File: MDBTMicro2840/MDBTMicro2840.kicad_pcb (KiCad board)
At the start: 2 copper layers, 33 x 18 mm, 25 parts, among them J1 USB_C_Receptacle_USB2.0, J2 SWD, U1 XC6220B331MR-G, U2 MDBT50Q-x1MV2, U3 TP4057, U4 ProMicro, X1 32.768kHz

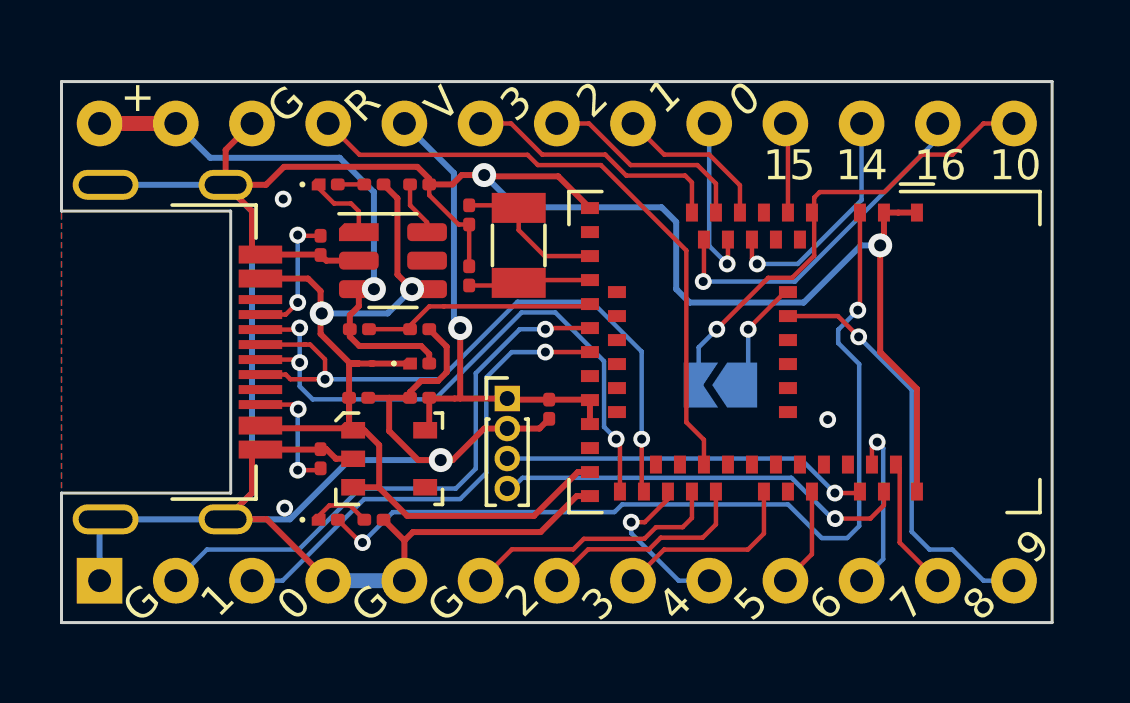
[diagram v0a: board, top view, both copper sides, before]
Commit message: Update 1N5819 footprint to SOD123
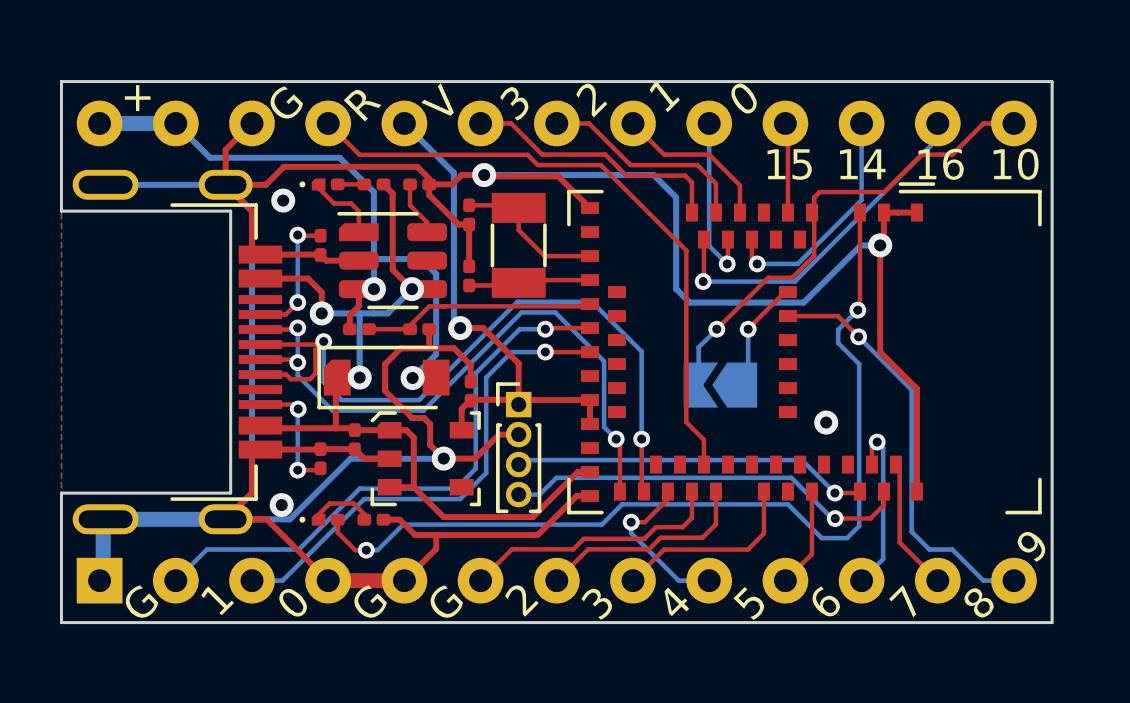
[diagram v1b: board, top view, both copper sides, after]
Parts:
- removed the C3 at (147.1, 103.5)
- D1: footprint Diode_SMD:D_0201_0603Metric -> Diode_SMD:D_SOD-123
- moved C4 1.72 mm to (144.4, 102.9), turned to -90 degrees
- moved C3 1.40 mm to (140.6, 104.5), turned to 90 degrees
- moved U1 1.22 mm to (142.9, 105.2)
- moved D1 1.19 mm to (141.7, 102.5)
- moved J2 0.43 mm to (146.1, 103.3)
- renumbered C4 to C3, C5 to C4, U3 to U2, U2 to U3
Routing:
- net VBAT: track 18.7 -> 22.2 mm, vias 1 -> 2
- net VBUS: track 33.4 -> 30.5 mm, vias 2 -> 3
- net USB_D+: track 22.9 -> 24.9 mm
- net GND: track 118.0 -> 119.6 mm

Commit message: Update silkscreen
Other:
- board text added: "A0"
- board text added: "A1"
- board text added: "A2"
- board text added: "A3"
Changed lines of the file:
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@@
-    (effects (font (size 1 1) (thickness 0.15)) (justify mirror))
-  )
-  (gr_text "Tx" (at 134.3 107.8) (layer "B.SilkS")
     (effects (font (size 1 1) (thickness 0.15)) (justify mirror))
   )
   (gr_text "1.13" (at 156.591 96.393 135) (layer "B.SilkS")
-    (effects (font (size 1 1) (thickness 0.15)) (justify mirror))
-  )
-  (gr_text "Rx" (at 138 107.8) (layer "B.SilkS")
     (effects (font (size 1 1) (thickness 0.15)) (justify mirror))
   )
@@
     (effects (font (size 1 1) (thickness 0.15)) (justify mirror))
   )
-  (gr_text "14" (at 157.48 95.377) (layer "F.SilkS")
+  (gr_text "A2" (at 147.32 95.504) (layer "F.SilkS")
+    (effects (font (size 1 1) (thickness 0.15) italic))
+  )
+  (gr_text "14" (at 157.48 95.504) (layer "F.SilkS")
     (effects (font (size 1 1) (thickness 0.15)))
   )
@@
     (effects (font (size 1 1) (thickness 0.15)))
   )
-  (gr_text "R" (at 140.843 93.345 45) (layer "F.SilkS")
+  (gr_text "A1\n" (at 149.9 95.504) (layer "F.SilkS")
+    (effects (font (size 1 1) (thickness 0.15) italic))
+  )
+  (gr_text "R" (at 140.8 93.3 45) (layer "F.SilkS")
     (effects (font (size 1 1) (thickness 0.15)))
   )
-  (gr_text "2" (at 146.177 109.855 45) (layer "F.SilkS")
+  (gr_text "2" (at 144.8 107.7) (layer "F.SilkS")
     (effects (font (size 1 1) (thickness 0.15)))
   )
-  (gr_text "V" (at 143.51 93.345 45) (layer "F.SilkS")
+  (gr_text "+" (at 135.636 93.218) (layer "F.SilkS")
     (effects (font (size 1 1) (thickness 0.15)))
   )
-  (gr_text "1" (at 150.876 93.091 45) (layer "F.SilkS")
+  (gr_text "V" (at 143.5 93.4 45) (layer "F.SilkS")
+    (effects (font (size 1 1) (thickness 0.15)))
+  )
+  (gr_text "15" (at 154.94 95.504) (layer "F.SilkS")
+    (effects (font (size 1 1) (thickness 0.15)))
+  )
+  (gr_text "8" (at 160.02 107.7) (layer "F.SilkS")
+    (effects (font (size 1 1) (thickness 0.15)))
+  )
+  (gr_text "10" (at 162.55 95.5) (layer "F.SilkS")
+    (effects (font (size 1 1) (thickness 0.15)))
+  )
+  (gr_text "G" (at 133.5 109.982 45) (layer "F.SilkS")
+    (effects (font (size 1 1) (thickness 0.15)))
+  )
+  (gr_text "A3" (at 144.8 95.504) (layer "F.SilkS")
     (effects (font (size 1 1) (thickness 0.15) italic))
   )
-  (gr_text "15" (at 155.067 95.377) (layer "F.SilkS")
+  (gr_text "9" (at 162.56 107.7) (layer "F.SilkS")
     (effects (font (size 1 1) (thickness 0.15)))
   )
-  (gr_text "0" (at 153.543 93.218 45) (layer "F.SilkS")
+  (gr_text "+" (at 133.096 93.218) (layer "F.SilkS")
+    (effects (font (size 1 1) (thickness 0.15)))
+  )
+  (gr_text "5" (at 152.4 107.696) (layer "F.SilkS")
+    (effects (font (size 1 1) (thickness 0.15)))
+  )
+  (gr_text "4" (at 149.86 107.7) (layer "F.SilkS")
+    (effects (font (size 1 1) (thickness 0.15)))
+  )
+  (gr_text "7" (at 157.6 107.696) (layer "F.SilkS")
+    (effects (font (size 1 1) (thickness 0.15)))
+  )
+  (gr_text "Tx" (at 134.62 107.8) (layer "F.SilkS")
+    (effects (font (size 1 1) (thickness 0.15)))
+  )
+  (gr_text "6" (at 154.94 107.696) (layer "F.SilkS")
+    (effects (font (size 1 1) (thickness 0.15)))
+  )
+  (gr_text "Rx" (at 138 107.8) (layer "F.SilkS")
+    (effects (font (size 1 1) (thickness 0.15)))
+  )
+  (gr_text "1" (at 135.9 109.855 45) (layer "F.SilkS")
+    (effects (font (size 1 1) (thickness 0.15)))
+  )
+  (gr_text "A0" (at 152.4 95.504) (layer "F.SilkS")
     (effects (font (size 1 1) (thickness 0.15) italic))
   )
-  (gr_text "8" (at 161.417 109.982 45) (layer "F.SilkS")
+  (gr_text "16" (at 160.02 95.504) (layer "F.SilkS")
     (effects (font (size 1 1) (thickness 0.15)))
   )
-  (gr_text "10" (at 162.6 95.377) (layer "F.SilkS")
+  (gr_text "G" (at 140.97 109.982 45) (layer "F.SilkS")
     (effects (font (size 1 1) (thickness 0.15)))
   )
-  (gr_text "G" (at 133.477 109.982 45) (layer "F.SilkS")
+  (gr_text "3" (at 147.32 107.7) (layer "F.SilkS")
     (effects (font (size 1 1) (thickness 0.15)))
   )
-  (gr_text "3" (at 145.923 93.345 45) (layer "F.SilkS")
-    (effects (font (size 1 1) (thickness 0.15) italic))
-  )
-  (gr_text "9" (at 163.195 108.077 45) (layer "F.SilkS")
+  (gr_text "0" (at 138.5 109.982 45) (layer "F.SilkS")
     (effects (font (size 1 1) (thickness 0.15)))
   )
-  (gr_text "+" (at 133.35 93.1) (layer "F.SilkS")
+  (gr_text "G" (at 143.5 109.982 45) (layer "F.SilkS")
     (effects (font (size 1 1) (thickness 0.15)))
   )
-  (gr_text "5" (at 153.797 109.982 45) (layer "F.SilkS")
-    (effects (font (size 1 1) (thickness 0.15)))
-  )
-  (gr_text "4" (at 151.257 109.982 45) (layer "F.SilkS")
-    (effects (font (size 1 1) (thickness 0.15)))
-  )
-  (gr_text "7" (at 159.004 109.982 45) (layer "F.SilkS")
-    (effects (font (size 1 1) (thickness 0.15)))
-  )
-  (gr_text "6" (at 156.3 109.982 45) (layer "F.SilkS")
-    (effects (font (size 1 1) (thickness 0.15)))
-  )
-  (gr_text "1" (at 136.017 109.855 45) (layer "F.SilkS")
-    (effects (font (size 1 1) (thickness 0.15)))
-  )
-  (gr_text "16" (at 160.1 95.377) (layer "F.SilkS")
-    (effects (font (size 1 1) (thickness 0.15)))
-  )
-  (gr_text "2" (at 148.463 93.218 45) (layer "F.SilkS")
-    (effects (font (size 1 1) (thickness 0.15) italic))
-  )
-  (gr_text "G" (at 141.097 109.982 45) (layer "F.SilkS")
-    (effects (font (size 1 1) (thickness 0.15)))
-  )
-  (gr_text "G" (at 143.637 109.982 45) (layer "F.SilkS")
-    (effects (font (size 1 1) (thickness 0.15)))
-  )
-  (gr_text "3" (at 148.717 109.982 45) (layer "F.SilkS")
-    (effects (font (size 1 1) (thickness 0.15)))
-  )
-  (gr_text "0" (at 138.557 109.982 45) (layer "F.SilkS")
-    (effects (font (size 1 1) (thickness 0.15)))
-  )

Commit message: Update footprint
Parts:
- J2: footprint Connector_PinHeader_1.00mm:PinHeader_1x04_P1.00mm_Vertical -> Connector_PinHeader_1.27mm:PinHeader_1x03_P1.27mm_Vertical
- moved C3 1.19 mm to (139.8, 105.5)
- moved C4 0.94 mm to (144.8, 102.0), turned to 0 degrees
- moved R7 0.92 mm to (138.7, 105.7), turned to -90 degrees
- moved U1 0.80 mm to (142.2, 105.2)
- moved J2 0.46 mm to (145.7, 103.7)
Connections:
- J2 pad 1: nRF_VDD -> GND
- J2 pad 2: GND -> SWDIO
- J2 pad 3: SWDIO -> SWCLK
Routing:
- net GND: track 119.6 -> 116.7 mm
- net VBUS: track 30.5 -> 31.6 mm
- net Net-(J1-PadB5): track 4.45 -> 3.50 mm
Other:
- board text added: "MDBTMicro-50Q v1.0"
- board text removed: "MDBTMicro2840 v1.0"

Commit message: Update sch
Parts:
- moved C1 2.03 mm to (144.4, 97.0), turned to 90 degrees
- moved C2 2.03 mm to (144.4, 99.1), turned to -90 degrees
- renumbered C2 to C1, C1 to C2
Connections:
- net /P1.13 renamed /P1.13/1.05
- C1 pad 2: Net-(C2-Pad2) -> Net-(U3-Pad17)
- C2 pad 2: Net-(C1-Pad2) -> Net-(C2-Pad2)
- U3 pad 17: Net-(C1-Pad2) -> Net-(U3-Pad17)
- X1 pad 2: Net-(C1-Pad2) -> Net-(U3-Pad17)
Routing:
- net Net-(U3-Pad17): track 0.00 -> 5.16 mm
- net Net-(C1-Pad2): track 5.16 -> 0.00 mm
